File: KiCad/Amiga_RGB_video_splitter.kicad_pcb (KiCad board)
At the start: 4 copper layers, 52.5 x 59 mm, 5 parts, among them J1 DB23_Female-Connector, J2 DB15_Female_HighDensity_Mount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, J3 KMDGX-9S-BS-1

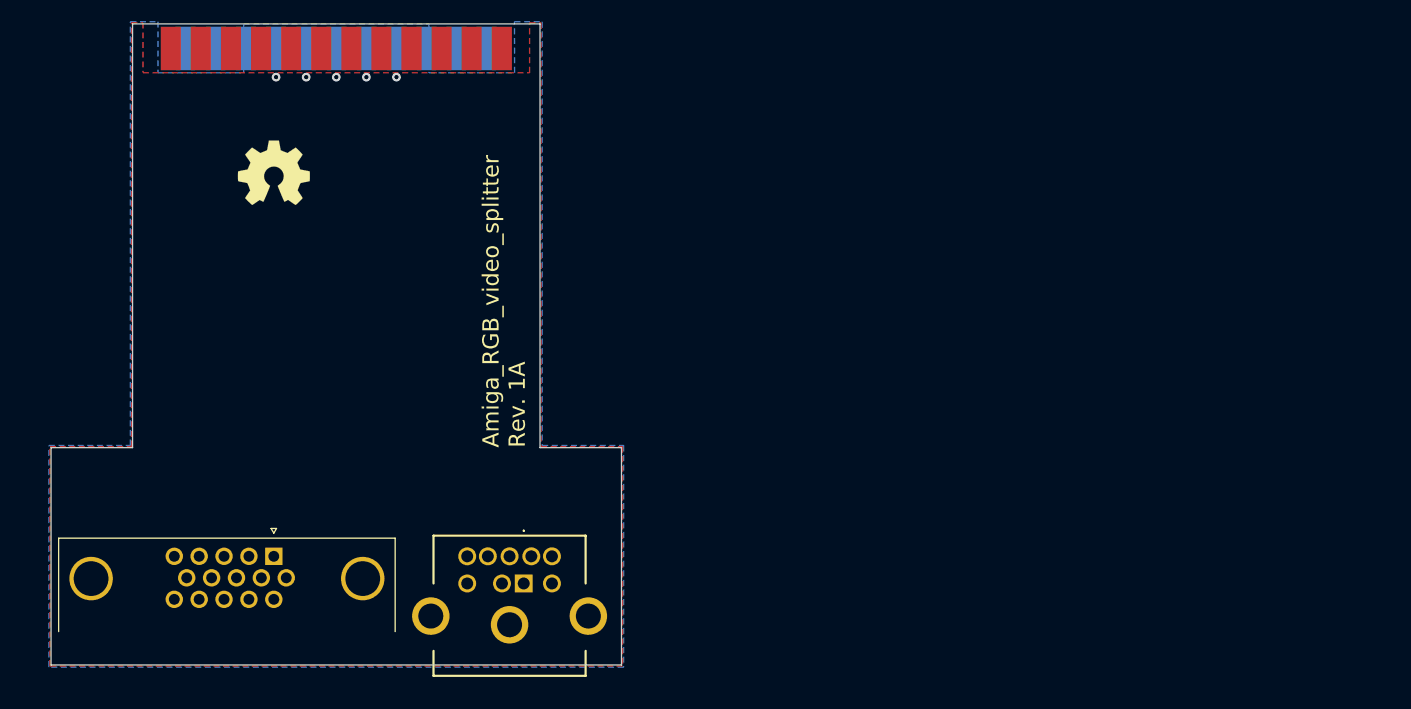
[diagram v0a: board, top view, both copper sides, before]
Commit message: Add a PJ-320A stereo input connector to the design
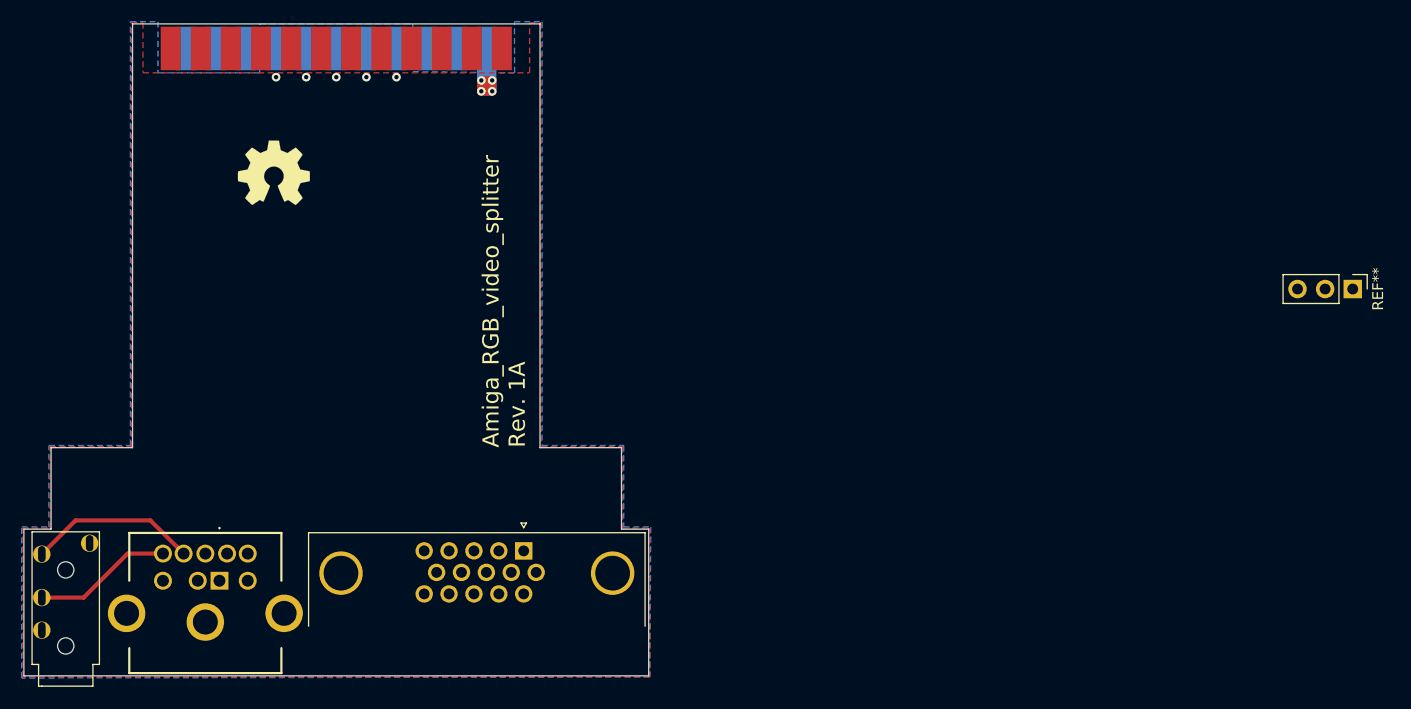
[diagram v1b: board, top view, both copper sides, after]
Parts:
- added J4: PJ-320A, Amiga_RGB_video_splitter:PJ-320A, F.Cu at (120.6, 145.9)
- added REF**: PinHeader_1x03_P2.54mm_Vertical, Connector_PinHeader_2.54mm:PinHeader_1x03_P2.54mm_Vertical, F.Cu at (241.2, 109.4)
- moved J3 28.0 mm to (136.9, 136.2)
- moved J2 23.0 mm to (164.9, 133.5)
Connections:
- net Net-(J1-Pad1) renamed XCLK
- net Net-(J1-Pad11) renamed HSYNC
- net Net-(J1-Pad12) renamed VSYNC
- net Net-(J1-Pad2) renamed XCLKEN
- net Net-(J1-Pad22) renamed /+12V
- J1 pad 10: Net-(J1-Pad10) -> /CSYNC
- J1 pad 23: Net-(J1-Pad23) -> VCC
- J1 pad 3: Net-(J1-Pad3) -> RED
- J1 pad 4: Net-(J1-Pad4) -> GREEN
- J1 pad 5: Net-(J1-Pad5) -> BLUE
- J3 pad 1: Net-(J3-Pad1) -> BLUE
- J3 pad 2: Net-(J3-Pad2) -> VCC
- J3 pad 3: Net-(J3-Pad3) -> GREEN
- J3 pad 4: Net-(J3-Pad4) -> /CSYNC
- J3 pad 7: Net-(J3-Pad7) -> RED
- J3 pad 8: Net-(J3-Pad8) -> AUDIO_L
- J3 pad 9: Net-(J3-Pad9) -> AUDIO_R
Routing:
- net VCC: track 0.00 -> 19.9 mm, vias 0 -> 4
- net AUDIO_L: track 0.00 -> 15.6 mm
- net AUDIO_R: track 0.00 -> 12.8 mm
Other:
- board size 52.5 x 59 mm -> 57.5 x 60 mm

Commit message: Add THS7374IPWR to the design and temporary routing
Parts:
- added U1: THS7374IPWR, Package_SO:TSSOP-14_4.4x5mm_P0.65mm, F.Cu at (147.7, 120.0)
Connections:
- J1 pad 3: RED -> AMIGA_R
- J1 pad 4: GREEN -> AMIGA_G
- J1 pad 5: BLUE -> AMIGA_B
- J2 pad 1: Net-(J2-Pad1) -> RED
- J2 pad 10: Net-(J2-Pad10) -> GND
- J2 pad 13: Net-(J2-Pad13) -> HSYNC
- J2 pad 14: Net-(J2-Pad14) -> VSYNC
- J2 pad 2: Net-(J2-Pad2) -> GREEN
- J2 pad 3: Net-(J2-Pad3) -> BLUE
- J2 pad 5: Net-(J2-Pad5) -> GND
- J2 pad 6: Net-(J2-Pad6) -> GND
- J2 pad 7: Net-(J2-Pad7) -> GND
- J2 pad 8: Net-(J2-Pad8) -> GND
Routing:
- net VSYNC: track 0.00 -> 68.0 mm
- net HSYNC: track 0.00 -> 63.0 mm
- net /CSYNC: track 0.00 -> 62.0 mm
- net BLUE: track 0.00 -> 39.3 mm
- net RED: track 0.00 -> 38.6 mm
- net GREEN: track 0.00 -> 37.4 mm
- net AMIGA_R: track 0.00 -> 34.2 mm
- net AMIGA_G: track 0.00 -> 33.3 mm
- net AMIGA_B: track 0.00 -> 32.4 mm
- net GND: vias 5 -> 6

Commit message: Add capacitor and route VCC to pin 10 on U1, add resistor R1 to Csync line
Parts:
- added C2: 0.1uF, Capacitor_SMD:C_0805_2012Metric_Pad1.18x1.45mm_HandSolder, F.Cu at (144.9, 125.2)
- added R1: R_Small, Resistor_SMD:R_1206_3216Metric_Pad1.30x1.75mm_HandSolder, F.Cu at (157.4, 94.4)
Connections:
- J3 pad 4: /CSYNC -> Net-(J3-Pad4)
- U1 pad 10: Net-(U1-Pad10) -> VCC
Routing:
- net /CSYNC: track 62.0 -> 5.59 mm
- net Net-(J3-Pad4): track 0.00 -> 53.3 mm
- net VCC: track 19.9 -> 31.4 mm, vias 4 -> 6
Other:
- board text added: "Amiga_RGB_video_splitter Rev. A"
- board text removed: "Amiga_RGB_video_splitter Rev. 1A"

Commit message: Add 75 Ω termination for RGB lines with resistor pack RN1
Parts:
- added RN1: R_Pack04 75 Ω, Amiga_RGB_video_splitter:RESCAF80P320X160X60-8N, F.Cu at (149.0, 111.6)
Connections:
- J1 pad 10: /CSYNC -> /CSYNK
- J3 pad 4: Net-(J3-Pad4) -> /CSYNC
- R1 pad 1: /CSYNC -> /CSYNK
- R1 pad 2: Net-(J3-Pad4) -> /CSYNC
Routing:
- net Net-(J3-Pad4): track 53.3 -> 0.00 mm
- net /CSYNC: track 5.59 -> 53.3 mm
- net /CSYNK: track 0.00 -> 5.59 mm
- net AMIGA_B: track 32.4 -> 35.6 mm
- net AMIGA_R: track 34.2 -> 35.8 mm
- net AMIGA_G: track 33.3 -> 34.6 mm
- net GND: vias 6 -> 12

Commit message: Add series resistor for VGA RGB lines with resistor pack RN2
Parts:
- added RN2: R_Pack04 75 Ω, Amiga_RGB_video_splitter:RESCAF80P320X160X60-8N, F.Cu at (155.8, 126.3)
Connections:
- net Net-(U1-Pad9) renamed BYPASS
- J2 pad 1: RED -> VGA_R
- J2 pad 2: GREEN -> VGA_G
- J2 pad 3: BLUE -> VGA_B
- U1 pad 6: Net-(U1-Pad6) -> GND
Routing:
- net RED: track 38.6 -> 26.8 mm
- net VGA_R: track 0.00 -> 11.5 mm
- net VGA_G: track 0.00 -> 9.62 mm
- net GREEN: track 37.4 -> 28.0 mm
- net VGA_B: track 0.00 -> 7.76 mm
- net BLUE: track 39.3 -> 32.3 mm

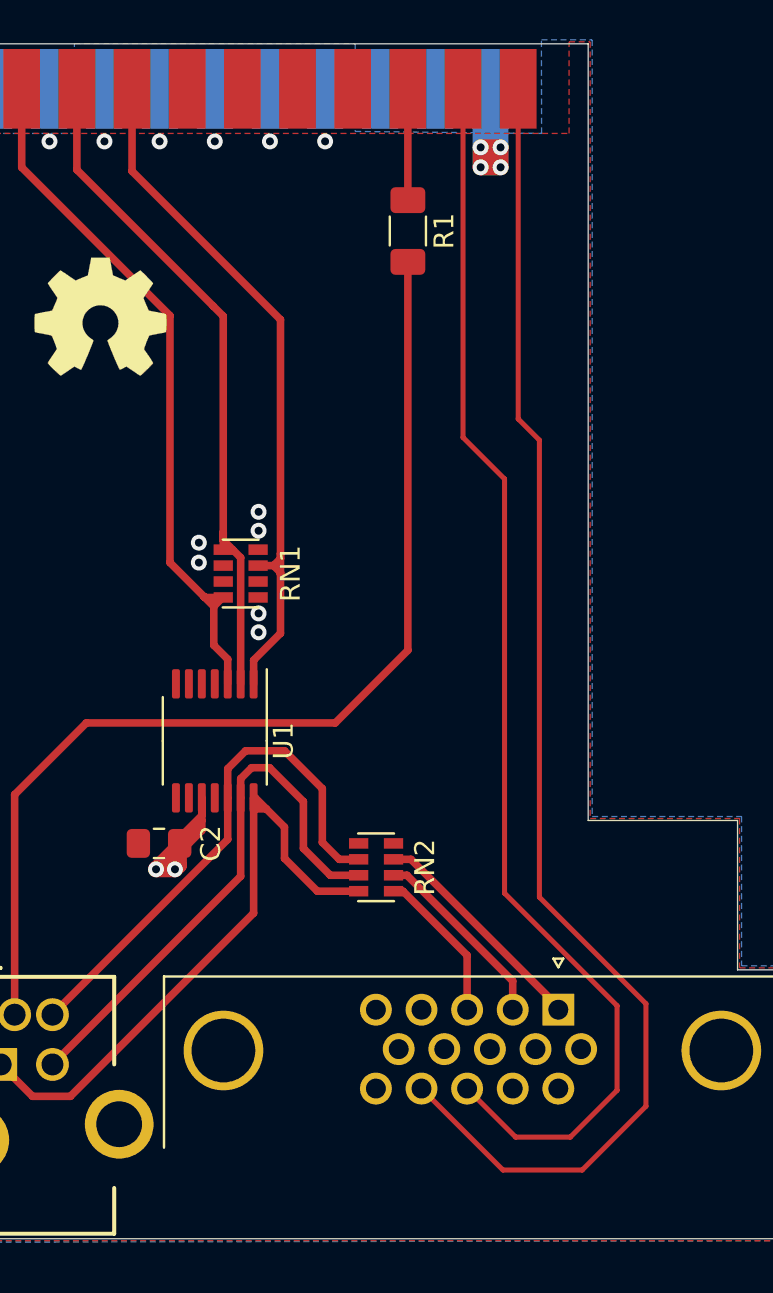
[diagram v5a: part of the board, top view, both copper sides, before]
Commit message: Add U2 (74HCT2G17) in TSOP-6 to the design for V-sync and H-sync buffering
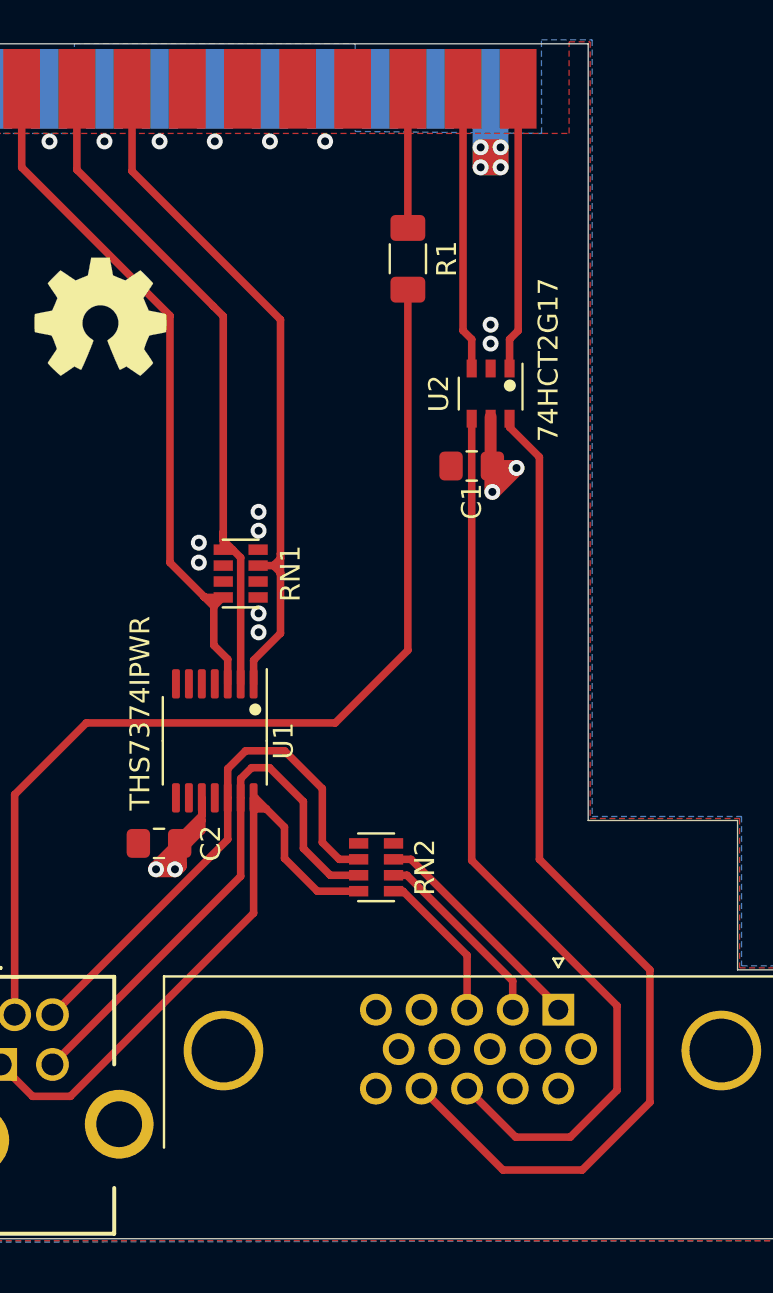
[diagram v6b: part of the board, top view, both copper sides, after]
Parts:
- added C1: 0.1uF, Capacitor_SMD:C_0805_2012Metric_Pad1.18x1.45mm_HandSolder, F.Cu at (160.6, 106.2)
- added U2: 74HCT2G17, Package_SO:TSOP-6_1.65x3.05mm_P0.95mm, F.Cu at (161.6, 102.6)
- moved R1 1.39 mm to (157.4, 95.8)
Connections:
- J1 pad 11: HSYNC -> /HSYNK
- J1 pad 12: VSYNC -> /VSYNK
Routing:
- net HSYNC: track 63.0 -> 46.3 mm
- net VSYNC: track 68.0 -> 51.8 mm
- net /HSYNK: track 0.00 -> 14.2 mm
- net /VSYNK: track 0.00 -> 14.2 mm
- net VCC: track 31.4 -> 38.2 mm, vias 6 -> 8
- net /CSYNK: track 5.59 -> 6.98 mm
- net /CSYNC: track 53.3 -> 51.9 mm
- net GND: vias 12 -> 14
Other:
- board text added: "74HCT2G17"
- board text added: "THS7374IPWR"

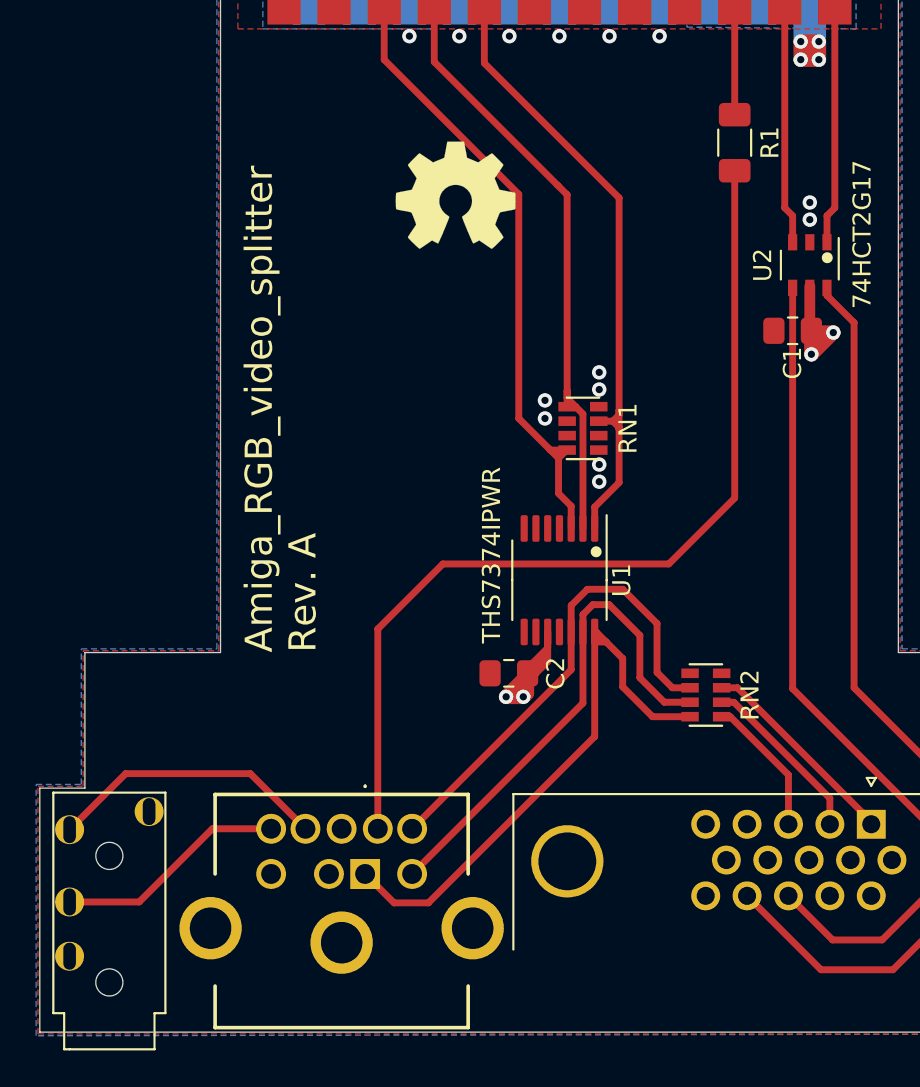
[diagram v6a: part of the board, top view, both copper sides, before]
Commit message: Change C1 to C2 and C2 to C3 and adding resistor Ohm values on silkscreen
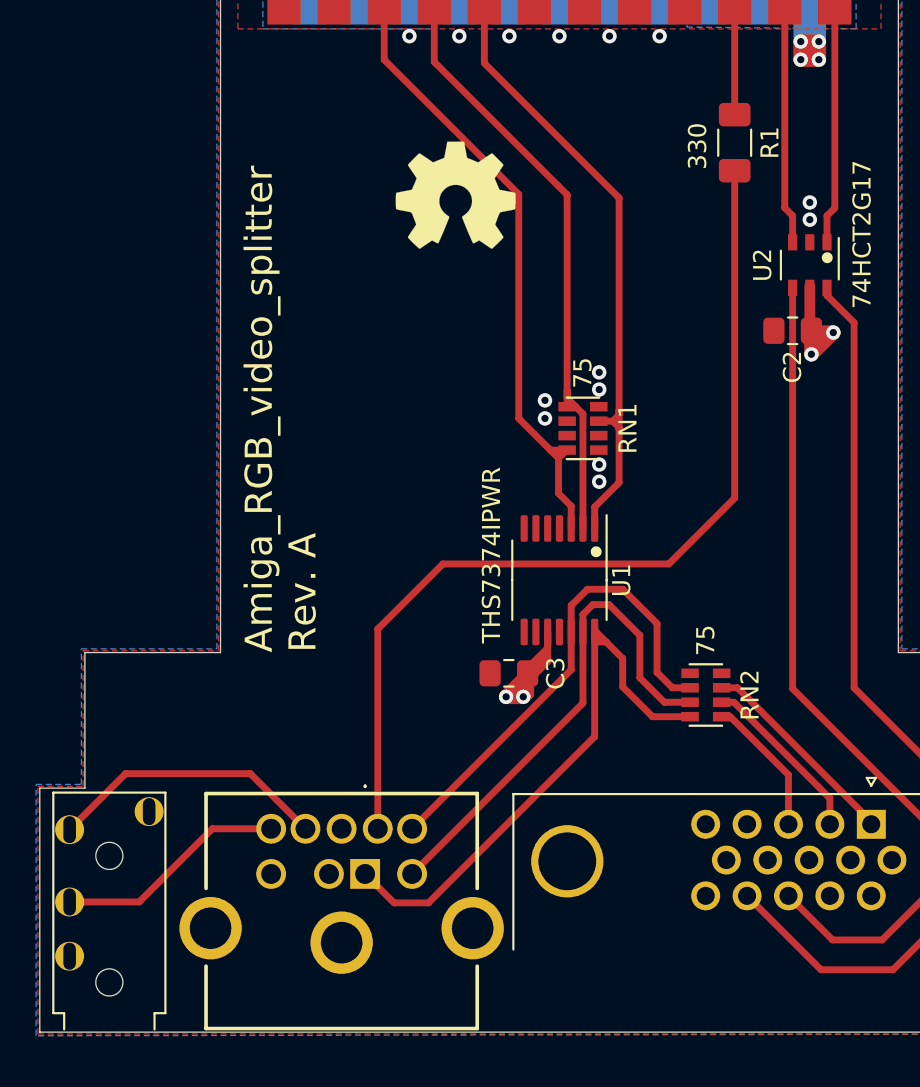
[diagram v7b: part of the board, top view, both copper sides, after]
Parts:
- renumbered C1 to C2, C2 to C3
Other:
- board text added: "330"
- board text added: "75"

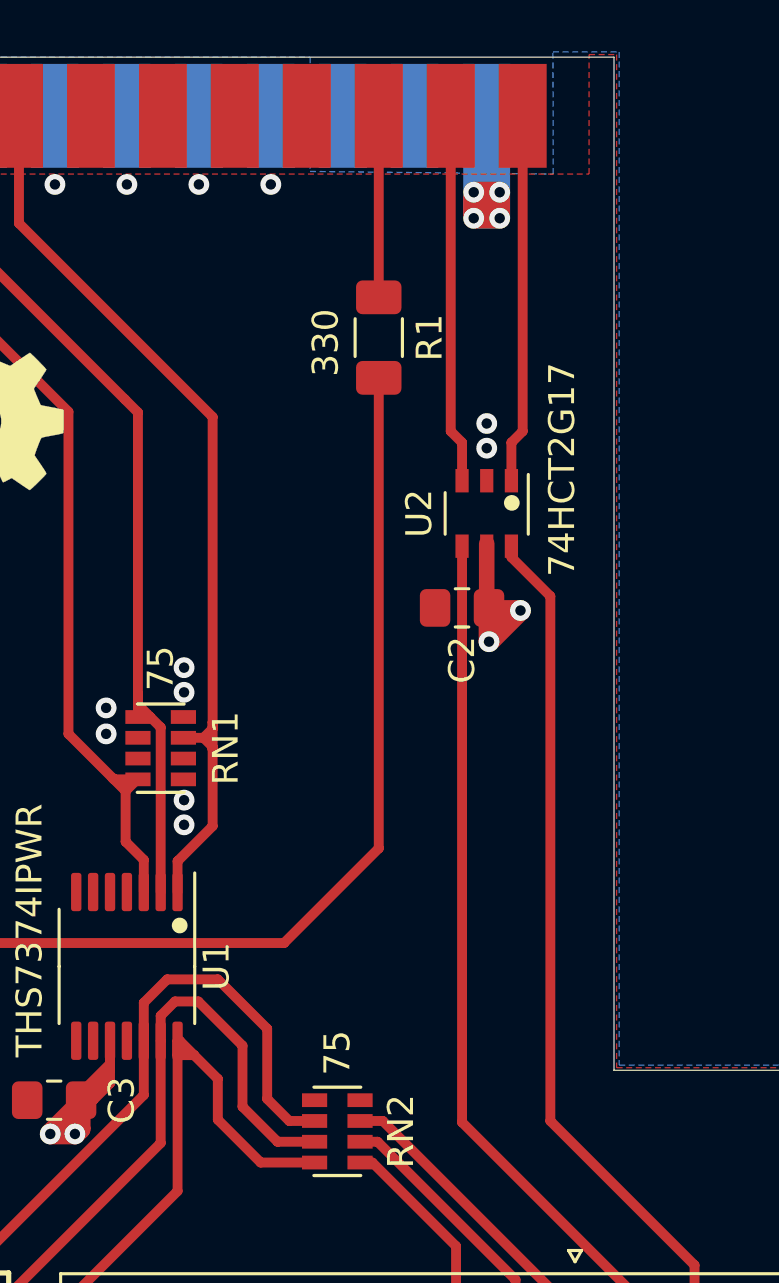
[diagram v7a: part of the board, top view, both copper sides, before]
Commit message: Add polarized TH-capacitor C1 100uF Radial pitch 2.5 mm
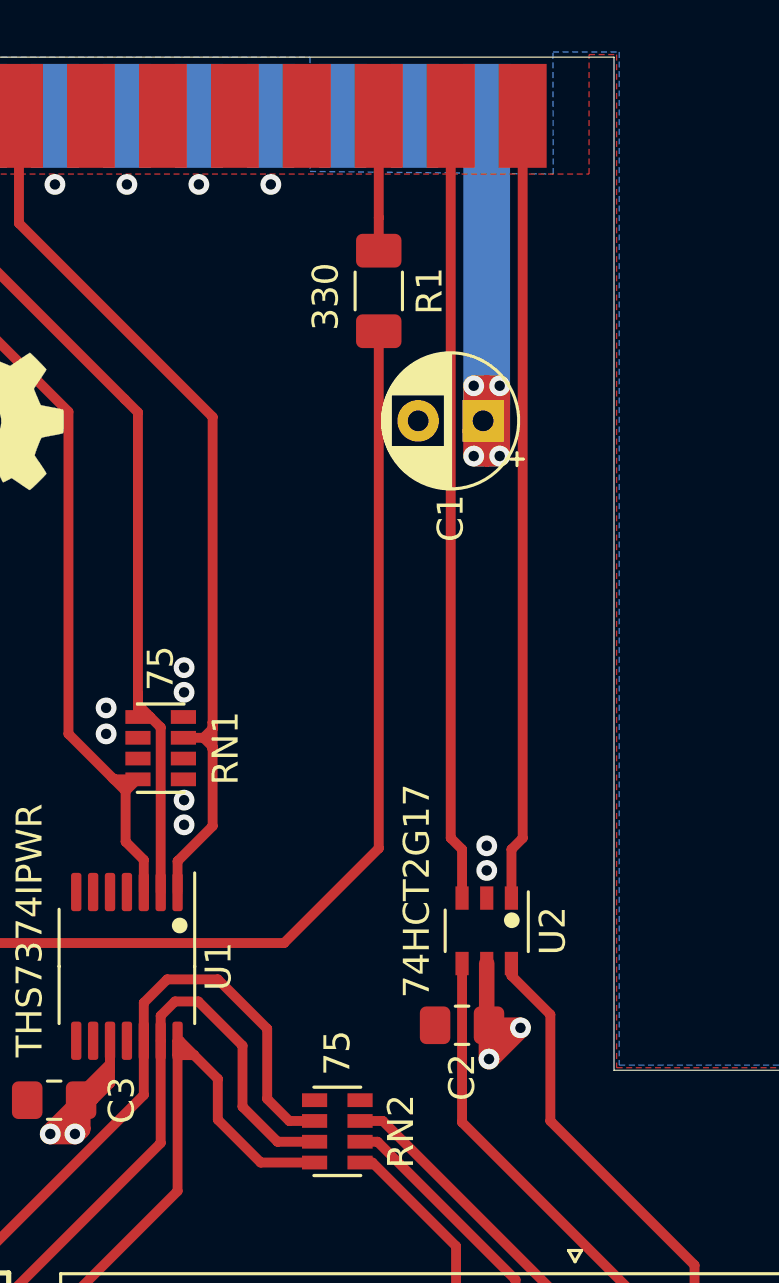
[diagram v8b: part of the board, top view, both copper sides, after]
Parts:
- added C1: 100uF Radial Pitch_2.5mm, Capacitor_THT:CP_Radial_D5.0mm_P2.50mm, F.Cu at (161.4, 99.0)
- moved C2 16.1 mm to (160.6, 122.3)
- moved U2 16.1 mm to (161.6, 118.6)
- moved R1 1.80 mm to (157.4, 94.0)
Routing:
- net VCC: track 38.2 -> 82.5 mm
- net VSYNC: track 51.8 -> 35.8 mm
- net HSYNC: track 46.3 -> 30.2 mm
- net /HSYNK: track 14.2 -> 30.3 mm
- net /VSYNK: track 14.2 -> 30.3 mm
- net /CSYNK: track 6.98 -> 5.19 mm
- net /CSYNC: track 51.9 -> 53.7 mm
